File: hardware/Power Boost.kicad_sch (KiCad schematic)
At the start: 0 parts

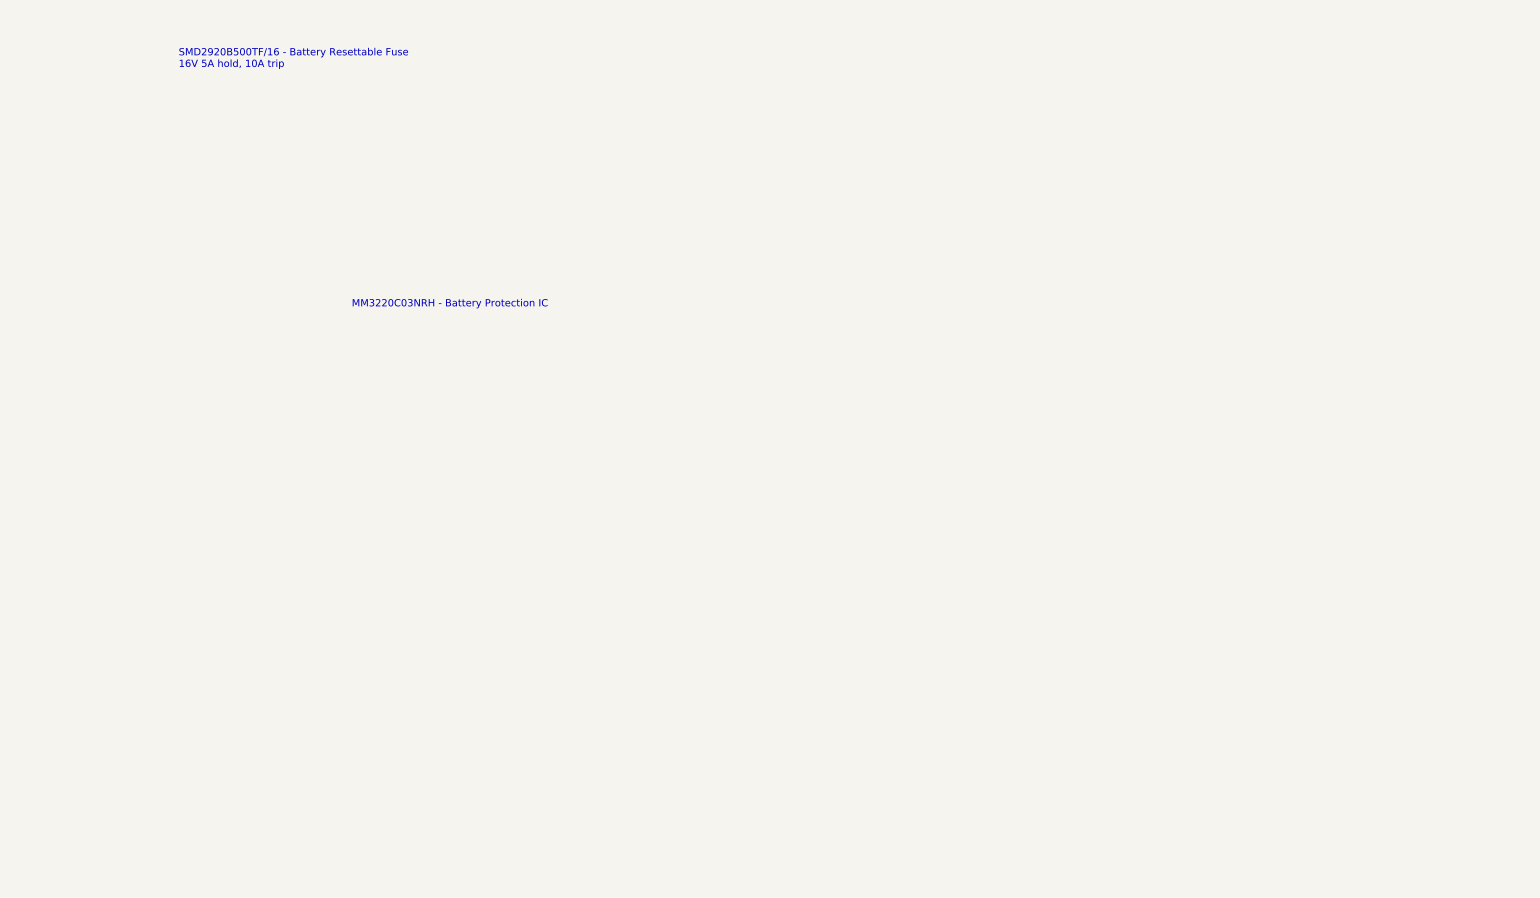
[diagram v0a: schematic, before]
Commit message: Hardware V0.2 - Schematics update
Combines Cell holder, BMS, and voltage regulator into single board
complete w. extensive electrical and thermal protections including:

* MM3220 BMS w Overvoltage, Overcurrent, undervoltage charging/discharge protect
* Fuses on cells, 12v in, 5v and 8.4v out.
* Reverse polarity protection on 12v and cells.

Adds debug UART header
Single IO header on every board
Minor component size corrections
Add current limiting resistor to RPI power NMOS gate.
Add optional support for MLCC/tantalum caps for Voltage Regulator instead of electrolytic
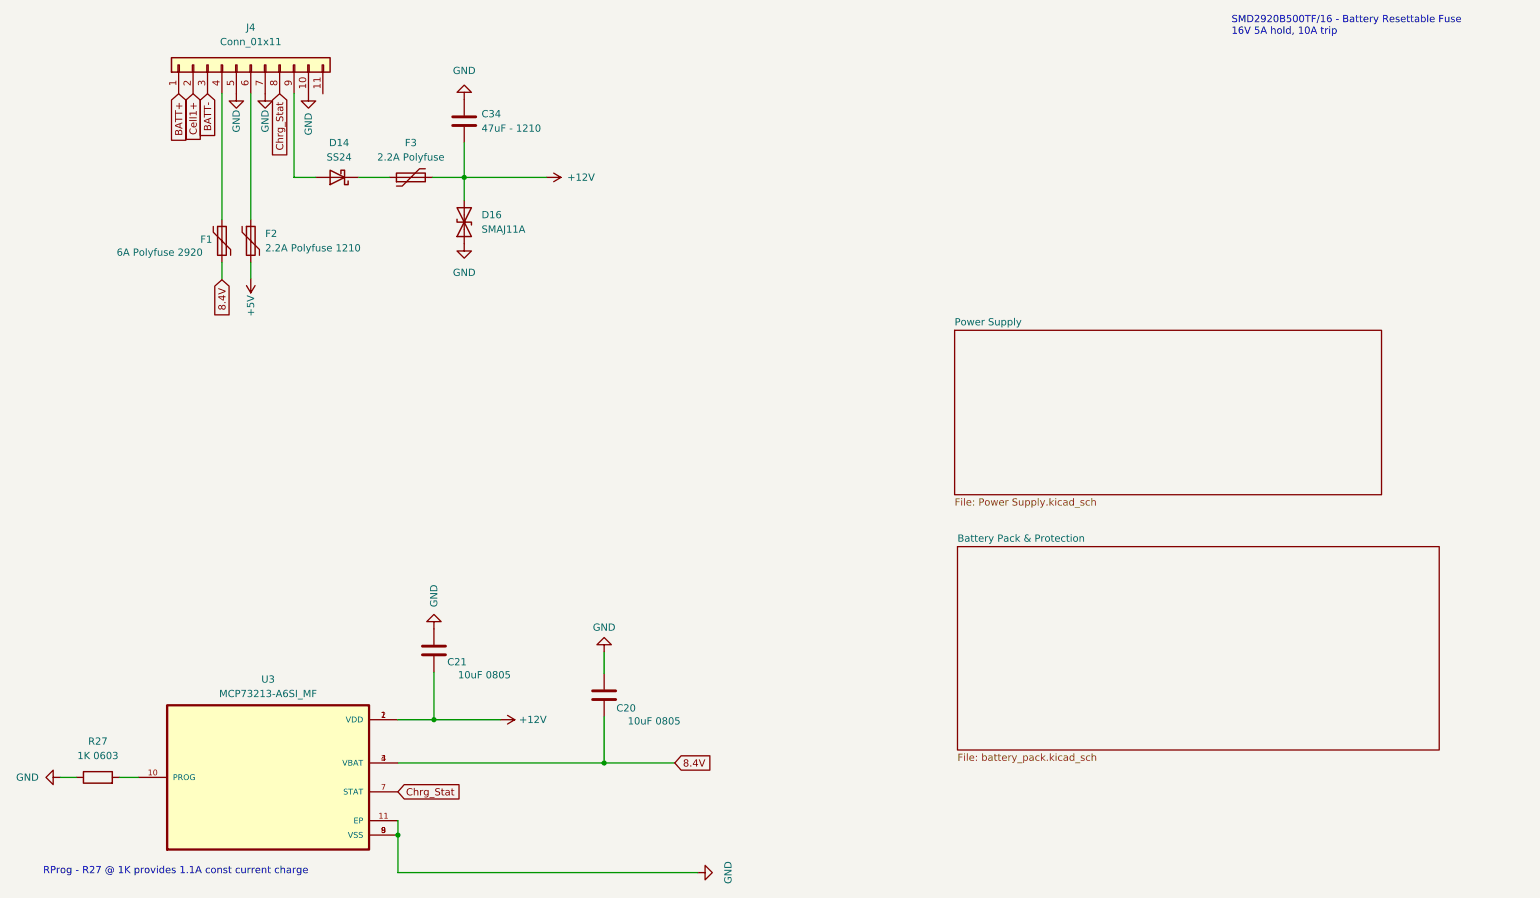
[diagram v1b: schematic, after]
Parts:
- added C20, C21: 10uF 0805, Capacitor_SMD:C_0603_1608Metric_Pad1.08x0.95mm_HandSolder, symbol Device:C
- added C34: 47uF - 1210, Resistor_SMD:R_1210_3225Metric_Pad1.30x2.65mm_HandSolder, symbol Device:C
- added D14: SS24, Diode_SMD:D_SMA_Handsoldering, symbol Device:D_Schottky
- added D16: SMAJ11A, Diode_SMD:D_SMA_Handsoldering, symbol Device:D_TVS
- added F1: 6A Polyfuse 2920, Fuse:Fuse_2920_7451Metric_Pad2.10x5.45mm_HandSolder, symbol Device:Polyfuse
- added F2: 2.2A Polyfuse 1210, Fuse:Fuse_1210_3225Metric_Pad1.42x2.65mm_HandSolder, symbol Device:Polyfuse
- added F3: 2.2A Polyfuse, Fuse:Fuse_1210_3225Metric_Pad1.42x2.65mm_HandSolder, symbol Device:Polyfuse
- added J4: Conn_01x11, Connector_PinSocket_2.54mm:PinSocket_1x11_P2.54mm_Vertical, symbol Connector_Generic:Conn_01x11
- added R27: 1K 0603, Resistor_SMD:R_0603_1608Metric, symbol Device:R
- added U3: MCP73213-A6SI_MF, MCP73213-A6SI_MF:SON50P300X300X100-11N, symbol MCP73213-A6SI_MF:MCP73213-A6SI_MF
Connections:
- new net: D14.1 (K), F3.1
- new net: F1.1, J4.4 (Pin_4)
- new net: R27.2, U3.10 (PROG)
- new net: D14.2 (A), J4.9 (Pin_9)
- new net: F2.1, J4.6 (Pin_6)
- new net +12V: C21.1, C34.2, D16.2 (A2), F3.2, U3.1 (VDD), U3.2 (VDD)
- new net +5V: F2.2
- new net 8.4V: C20.1, F1.2, U3.3 (VBAT), U3.4 (VBAT)
- new net BATT+: J4.1 (Pin_1)
- new net BATT-: J4.3 (Pin_3)
- new net Cell1+: J4.2 (Pin_2)
- new net Chrg_Stat: J4.8 (Pin_8), U3.7 (STAT)
- new net GND: C20.2, C21.2, C34.1, D16.1 (A1), J4.10 (Pin_10), J4.5 (Pin_5), J4.7 (Pin_7), R27.1, U3.11 (EP), U3.8 (VSS), U3.9 (VSS)
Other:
- added sheet Battery Pack & Protection (battery_pack.kicad_sch)
- added sheet Power Supply (Power Supply.kicad_sch)
- note added: "RProg - R27 @ 1K provides 1.1A const current charge"
- note removed: "MM3220C03NRH - Battery Protection IC"

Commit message: Hardware revision 0.2 routing
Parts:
- removed F2: 2.2A Polyfuse 1210, Fuse:Fuse_1210_3225Metric_Pad1.42x2.65mm_HandSolder, symbol Device:Polyfuse
- J4: footprint Connector_PinSocket_2.54mm:PinSocket_1x11_P2.54mm_Vertical -> Board:Board_outline
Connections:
- net BATT+ is gone; now on net 8.4V Out: J4.1 (Pin_1)
- net +5V: now also J4.6 (Pin_6)
- net 8.4V Out: now reaches F1.1, J4.4 (Pin_4)
- net BATT-: no longer names the net of J4.3 (Pin_3)
- net Cell1+ renamed BATT_LVL_MID
- no-connect marks 0 -> 2
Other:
- note removed: "SMD2920B500TF/16 - Battery Resettable Fuse 16V 5A hold, 10A trip"
- company: (none) -> KBader94
- title: (none) -> OpenActionCam
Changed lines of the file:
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@@
 (kicad_sch (version 20230121) (generator eeschema)
   (paper "A4")
+  (title_block
+    (title "OpenActionCam")
+    (date "2025-04-10")
+    (rev "0.2")
+    (company "KBader94")
+    (comment 1 "https://github.com/kbader94/OpenActionCam")
+  )
   (junction (at 121.92 156.21) (diameter 0) (color 0 0 0 0)
   )
+  (junction (at 54.61 57.404) (diameter 0) (color 0 0 0 0)
+  )
   (junction (at 97.282 53.086) (diameter 0) (color 0 0 0 0)
   )
@@
   (junction (at 85.598 168.91) (diameter 0) (color 0 0 0 0)
   )
+  (no_connect (at 72.39 38.354))
+  (no_connect (at 52.07 38.354))
   (wire (pts (xy 54.61 71.12) (xy 54.61 68.072))
     (stroke (width 0) (type default))
@@
     (stroke (width 0) (type default))
   )
+  (wire (pts (xy 46.99 57.404) (xy 54.61 57.404))
+    (stroke (width 0) (type default))
+  )
   (wire (pts (xy 85.598 148.59) (xy 91.948 148.59))
     (stroke (width 0) (type default))
@@
     (stroke (width 0) (type default))
   )
-  (wire (pts (xy 59.69 60.452) (xy 59.69 38.354))
+  (wire (pts (xy 59.69 38.354) (xy 59.69 70.866))
     (stroke (width 0) (type default))
   )
@@
     (stroke (width 0) (type default))
   )
+  (wire (pts (xy 46.99 38.354) (xy 46.99 57.404))
+    (stroke (width 0) (type default))
+  )
   (wire (pts (xy 67.31 53.086) (xy 67.31 38.354))
     (stroke (width 0) (type default))
@@
     (stroke (width 0) (type default))
   )
-  (wire (pts (xy 54.61 38.354) (xy 54.61 60.452))
-    (stroke (width 0) (type default))
-  )
-  (wire (pts (xy 59.69 70.866) (xy 59.69 68.072))
+  (wire (pts (xy 54.61 38.354) (xy 54.61 57.404))
+    (stroke (width 0) (type default))
+  )
+  (wire (pts (xy 54.61 57.404) (xy 54.61 60.452))
     (stroke (width 0) (type default))
   )
@@
   (wire (pts (xy 97.282 53.086) (xy 97.282 57.15))
     (stroke (width 0) (type default))
-  )
-  (text "SMD2920B500TF/16 - Battery Resettable Fuse\n16V 5A hold, 10A trip"
-    (at 232.41 28.194 0)
-    (effects (font (size 1.27 1.27)) (justify left bottom))
   )
   (text "RProg - R27 @ 1K provides 1.1A const current charge\n"
@@
     (effects (font (size 1.27 1.27)) (justify left bottom))
   )
-  (global_label "BATT-" (shape input) (at 52.07 38.354 270) (fields_autoplaced)
-    (effects (font (size 1.27 1.27)) (justify right))
-    (property "Intersheetrefs" "${INTERSHEET_REFS}" (at 52.07 47.3005 90)
-      (effects (font (size 1.27 1.27)) (justify right) hide)
-    )
+  (label "8.4V Out" (at 46.99 52.578 90) (fields_autoplaced)
+    (effects (font (size 1.27 1.27)) (justify left bottom))
   )
   (global_label "8.4V" (shape input) (at 134.366 156.21 0) (fields_autoplaced)
@@
     )
   )
-  (global_label "Cell1+" (shape input) (at 49.53 38.354 270) (fields_autoplaced)
+  (global_label "BATT_LVL_MID" (shape input) (at 49.53 38.354 270) (fields_autoplaced)
     (effects (font (size 1.27 1.27)) (justify right))
-    (property "Intersheetrefs" "${INTERSHEET_REFS}" (at 49.53 47.9052 90)
-      (effects (font (size 1.27 1.27)) (justify right) hide)
-    )
-  )
-  (global_label "BATT+" (shape input) (at 46.99 38.354 270) (fields_autoplaced)
-    (effects (font (size 1.27 1.27)) (justify right))
-    (property "Intersheetrefs" "${INTERSHEET_REFS}" (at 46.99 47.3005 90)
+    (property "Intersheetrefs" "${INTERSHEET_REFS}" (at 49.53 54.1343 90)
       (effects (font (size 1.27 1.27)) (justify right) hide)
     )
@@
     (pin "1")
     (instances
-      (project "iJet"
+      (project "OAC"
         (path "/e63e39d7-6ac0-4ffd-8aa3-1841a4541b55/800e290e-8cfb-4946-9373-3e863e65a993"
           (reference "#PWR059") (unit 1)
@@
     (pin "1")
     (instances
-      (project "iJet"
+      (project "OAC"
         (path "/e63e39d7-6ac0-4ffd-8aa3-1841a4541b55/800e290e-8cfb-4946-9373-3e863e65a993"
           (reference "C34") (unit 1)
@@
     (pin "1")
     (instances
-      (project "iJet"
+      (project "OAC"
         (path "/e63e39d7-6ac0-4ffd-8aa3-1841a4541b55/800e290e-8cfb-4946-9373-3e863e65a993"
           (reference "#PWR042") (unit 1)
@@
     (pin "2")
     (instances
-      (project "iJet"
+      (project "OAC"
         (path "/e63e39d7-6ac0-4ffd-8aa3-1841a4541b55/800e290e-8cfb-4946-9373-3e863e65a993"
           (reference "F3") (unit 1)
@@
     (pin "1")
     (instances
-      (project "iJet"
+      (project "OAC"
         (path "/e63e39d7-6ac0-4ffd-8aa3-1841a4541b55/800e290e-8cfb-4946-9373-3e863e65a993"
           (reference "#PWR039") (unit 1)
@@
     (pin "1")
     (instances
-      (project "iJet"
+      (project "OAC"
         (path "/e63e39d7-6ac0-4ffd-8aa3-1841a4541b55/800e290e-8cfb-4946-9373-3e863e65a993"
           (reference "#PWR028") (unit 1)
@@
     (pin "1")
     (instances
-      (project "iJet"
+      (project "OAC"
         (path "/e63e39d7-6ac0-4ffd-8aa3-1841a4541b55/800e290e-8cfb-4946-9373-3e863e65a993"
           (reference "#PWR040") (unit 1)
@@
     (pin "1")
     (instances
-      (project "iJet"
+      (project "OAC"
         (path "/e63e39d7-6ac0-4ffd-8aa3-1841a4541b55/800e290e-8cfb-4946-9373-3e863e65a993"
           (reference "#PWR070") (unit 1)
@@
     (pin "1")
     (instances
-      (project "iJet"
+      (project "OAC"
         (path "/e63e39d7-6ac0-4ffd-8aa3-1841a4541b55/800e290e-8cfb-4946-9373-3e863e65a993"
           (reference "#PWR014") (unit 1)
@@
     (pin "2")
     (instances
-      (project "iJet"
+      (project "OAC"
         (path "/e63e39d7-6ac0-4ffd-8aa3-1841a4541b55/800e290e-8cfb-4946-9373-3e863e65a993"
           (reference "D16") (unit 1)
@@
     (pin "2")
     (instances
-      (project "iJet"
+      (project "OAC"
         (path "/e63e39d7-6ac0-4ffd-8aa3-1841a4541b55/800e290e-8cfb-4946-9373-3e863e65a993"
           (reference "C20") (unit 1)
@@
     (pin "1")
     (instances
-      (project "iJet"
+      (project "OAC"
         (path "/e63e39d7-6ac0-4ffd-8aa3-1841a4541b55/800e290e-8cfb-4946-9373-3e863e65a993"
           (reference "#PWR022") (unit 1)
@@
     (pin "1")
     (instances
-      (project "iJet"
+      (project "OAC"
         (path "/e63e39d7-6ac0-4ffd-8aa3-1841a4541b55/800e290e-8cfb-4946-9373-3e863e65a993"
           (reference "#PWR030") (unit 1)
@@
     (pin "2")
     (instances
-      (project "iJet"
+      (project "OAC"
         (path "/e63e39d7-6ac0-4ffd-8aa3-1841a4541b55/800e290e-8cfb-4946-9373-3e863e65a993"
           (reference "F1") (unit 1)
@@
     (pin "2")
     (instances
-      (project "iJet"
+      (project "OAC"
         (path "/e63e39d7-6ac0-4ffd-8aa3-1841a4541b55/800e290e-8cfb-4946-9373-3e863e65a993"
           (reference "U3") (unit 1)
@@
     (pin "2")
     (instances
-      (project "iJet"
+      (project "OAC"
         (path "/e63e39d7-6ac0-4ffd-8aa3-1841a4541b55/800e290e-8cfb-4946-9373-3e863e65a993"
           (reference "C21") (unit 1)
@@
     (pin "1")
     (instances
-      (project "iJet"
+      (project "OAC"
         (path "/e63e39d7-6ac0-4ffd-8aa3-1841a4541b55/800e290e-8cfb-4946-9373-3e863e65a993"
           (reference "D14") (unit 1)
@@
     (pin "1")
     (instances
-      (project "iJet"
+      (project "OAC"
         (path "/e63e39d7-6ac0-4ffd-8aa3-1841a4541b55/800e290e-8cfb-4946-9373-3e863e65a993"
           (reference "#PWR041") (unit 1)
@@
     )
   )
-  (symbol (lib_id "Device:Polyfuse") (at 59.69 64.262 0) (unit 1)
-    (in_bom yes) (on_board yes) (dnp no) (fields_autoplaced)
-    (property "Reference" "F2" (at 62.23 62.992 0)
-      (effects (font (size 1.27 1.27)) (justify left))
-    )
-    (property "Value" "2.2A Polyfuse 1210" (at 62.23 65.532 0)
-      (effects (font (size 1.27 1.27)) (justify left))
-    )
-    (property "Footprint" "Fuse:Fuse_1210_3225Metric_Pad1.42x2.65mm_HandSolder" (at 60.96 69.342 0)
-      (effects (font (size 1.27 1.27)) (justify left) hide)
-    )
-    (property "Datasheet" "~" (at 59.69 64.262 0)
-      (effects (font (size 1.27 1.27)) hide)
-    )
-    (pin "2")
-    (pin "1")
-    (instances
-      (project "iJet"
-        (path "/e63e39d7-6ac0-4ffd-8aa3-1841a4541b55/800e290e-8cfb-4946-9373-3e863e65a993"
-          (reference "F2") (unit 1)
-        )
-      )
-    )
-  )
   (symbol (lib_id "Device:R") (at 32.766 158.75 90) (unit 1)
     (in_bom yes) (on_board yes) (dnp no) (fields_autoplaced)
@@
     (pin "1")
     (instances
-      (project "iJet"
+      (project "OAC"
         (path "/e63e39d7-6ac0-4ffd-8aa3-1841a4541b55/800e290e-8cfb-4946-9373-3e863e65a993"
           (reference "R27") (unit 1)
@@
       (effects (font (size 1.27 1.27)))
     )
-    (property "Footprint" "Connector_PinSocket_2.54mm:PinSocket_1x11_P2.54mm_Vertical" (at 59.69 33.274 0)
+    (property "Footprint" "Board:Board_outline" (at 59.69 33.274 0)
       (effects (font (size 1.27 1.27)) hide)
     )
@@
     (pin "6")
     (instances
-      (project "iJet"
+      (project "OAC"
         (path "/e63e39d7-6ac0-4ffd-8aa3-1841a4541b55/800e290e-8cfb-4946-9373-3e863e65a993"
           (reference "J4") (unit 1)
@@
     (pin "1")
     (instances
-      (project "iJet"
+      (project "OAC"
         (path "/e63e39d7-6ac0-4ffd-8aa3-1841a4541b55/800e290e-8cfb-4946-9373-3e863e65a993"
           (reference "#PWR044") (unit 1)
@@
     (pin "1")
     (instances
-      (project "iJet"
+      (project "OAC"
         (path "/e63e39d7-6ac0-4ffd-8aa3-1841a4541b55/800e290e-8cfb-4946-9373-3e863e65a993"
           (reference "#PWR031") (unit 1)
@@
     )
     (instances
-      (project "iJet"
+      (project "OAC"
         (path "/e63e39d7-6ac0-4ffd-8aa3-1841a4541b55/800e290e-8cfb-4946-9373-3e863e65a993" (page "7"))
       )
@@
     )
     (instances
-      (project "iJet"
+      (project "OAC"
         (path "/e63e39d7-6ac0-4ffd-8aa3-1841a4541b55" (page "6"))
         (path "/e63e39d7-6ac0-4ffd-8aa3-1841a4541b55/800e290e-8cfb-4946-9373-3e863e65a993" (page "2"))
